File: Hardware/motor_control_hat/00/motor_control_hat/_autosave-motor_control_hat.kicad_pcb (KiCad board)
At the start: 4 copper layers, 115 x 100 mm, 34 parts, among them P1 TB_1x2_5.08mm_RA, P10 X9254WR-04-N0SN, P11 X9254WR-04-N0SN, P12 X9254WR-04-N0SN, P13 X9254WR-04-N0SN, P2 TB_1x2_5.08mm_RA, P3 TB_1x2_5.08mm_RA, P4 TB_1x2_5.08mm_RA, P5 X9254WR-04-N0SN, P6 X9254WR-04-N0SN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

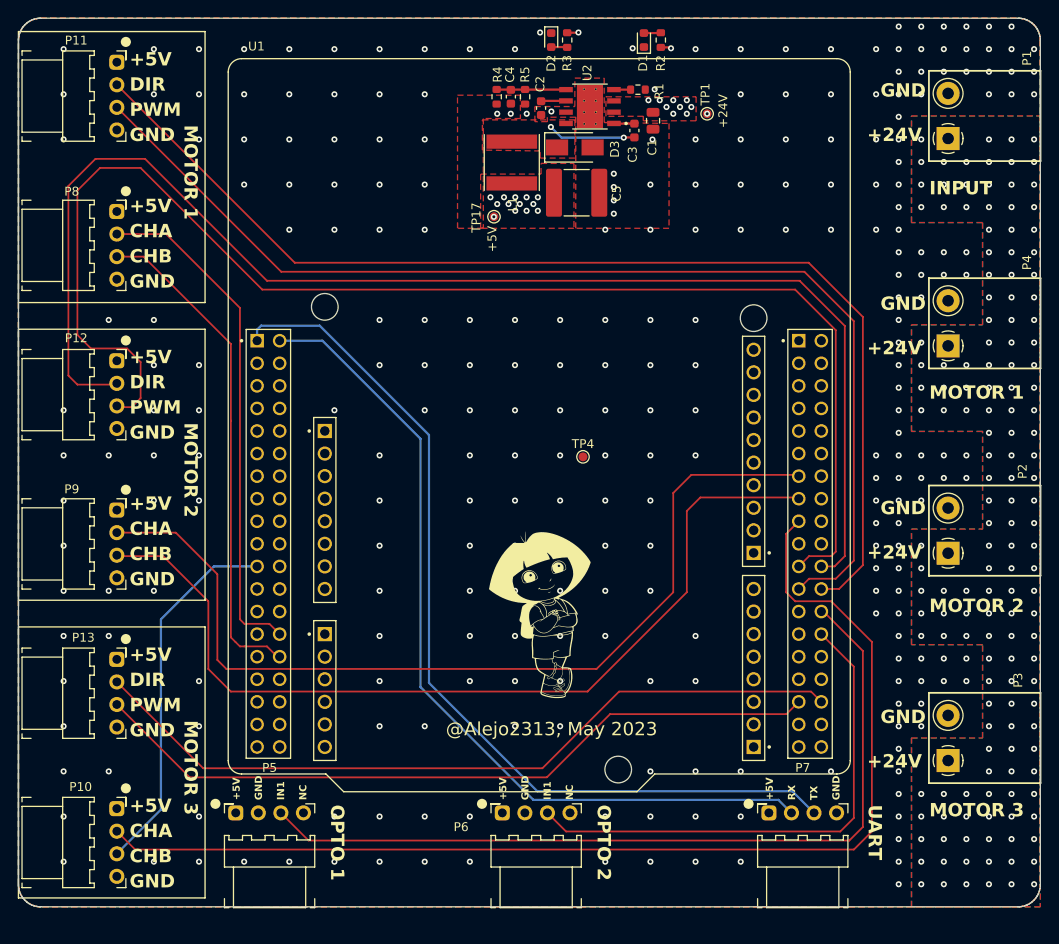
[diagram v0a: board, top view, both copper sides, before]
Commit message: Motor hat V0 created
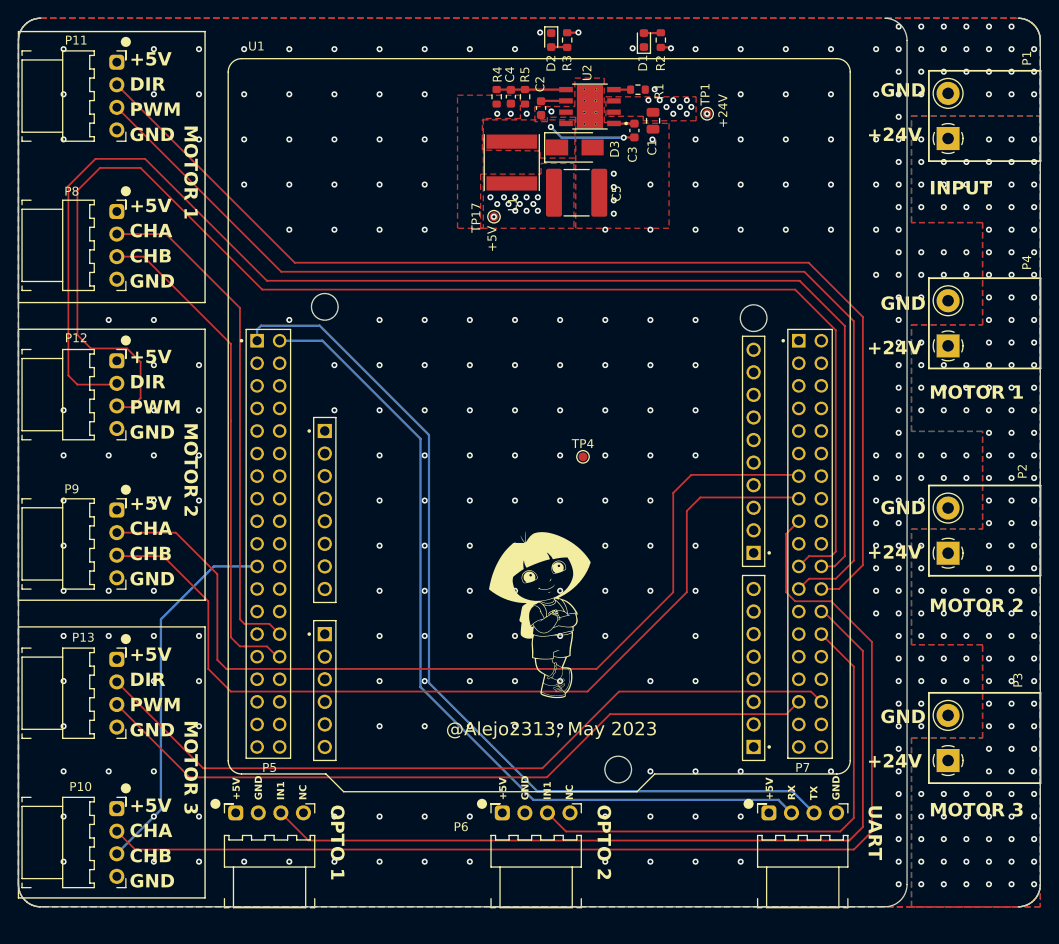
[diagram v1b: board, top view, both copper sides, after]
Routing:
- net GND: vias 279 -> 297
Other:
- outline, holes or cut-outs redrawn

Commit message: Power connectors removed
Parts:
- removed P2, P3, P4: TB_1x2_5.08mm_RA, PluggableTerminalBLock:MX2EDGR-5.08-GN01-02P-Cu-A
- moved P1 80.2 mm to (153.0, 126.4), turned to 0 degrees
- moved P7 60.0 mm to (93.8, 126.4)
- moved P5 20.0 mm to (113.8, 126.4)
- moved P6 12.5 mm to (136.3, 126.4)
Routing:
- net /USART3_TX: track 103.2 -> 74.8 mm
- net /USART3_RX: track 96.0 -> 70.0 mm
- net /OC_IN_1: track 93.7 -> 75.8 mm
- net /OC_IN_2: track 58.2 -> 48.3 mm
- net /ENC3_PHA: track 128.5 -> 130.6 mm
- net GND: vias 297 -> 184
- net +24V: vias 159 -> 11
- removed copper zone on B.Cu, net +24V
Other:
- board size 115 x 100 mm -> 100 x 100 mm
- board text removed: "+24V"
- board text removed: "INPUT"
